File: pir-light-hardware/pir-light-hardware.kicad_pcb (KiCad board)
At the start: 2 copper layers, 29.1 x 32.2 mm, 28 parts, among them J1 ZH1.5-3, J2 ZH1.5-3, Q1 AON7240, U1 M74VHC1GT08DFT2G, U2 LMV331IDCKR

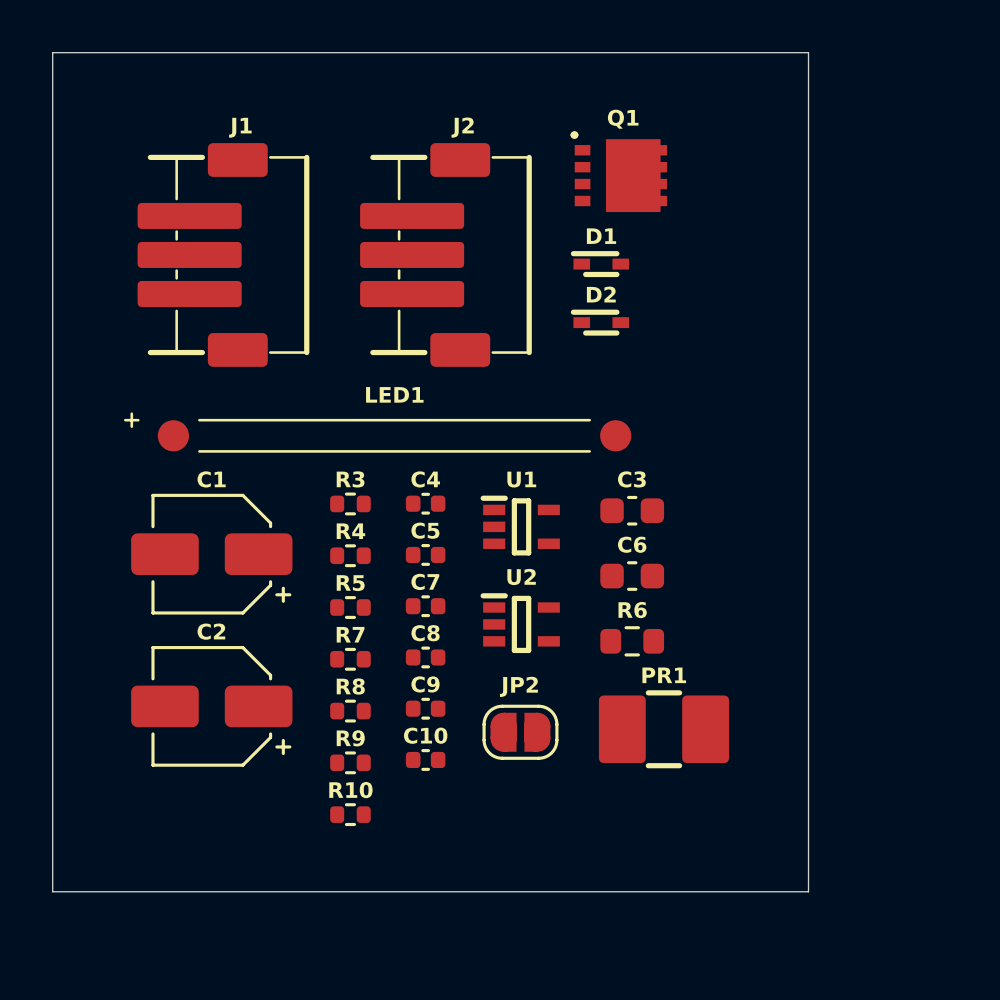
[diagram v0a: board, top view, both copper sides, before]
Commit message: chore: rework sustain feature, add actual components to schematic
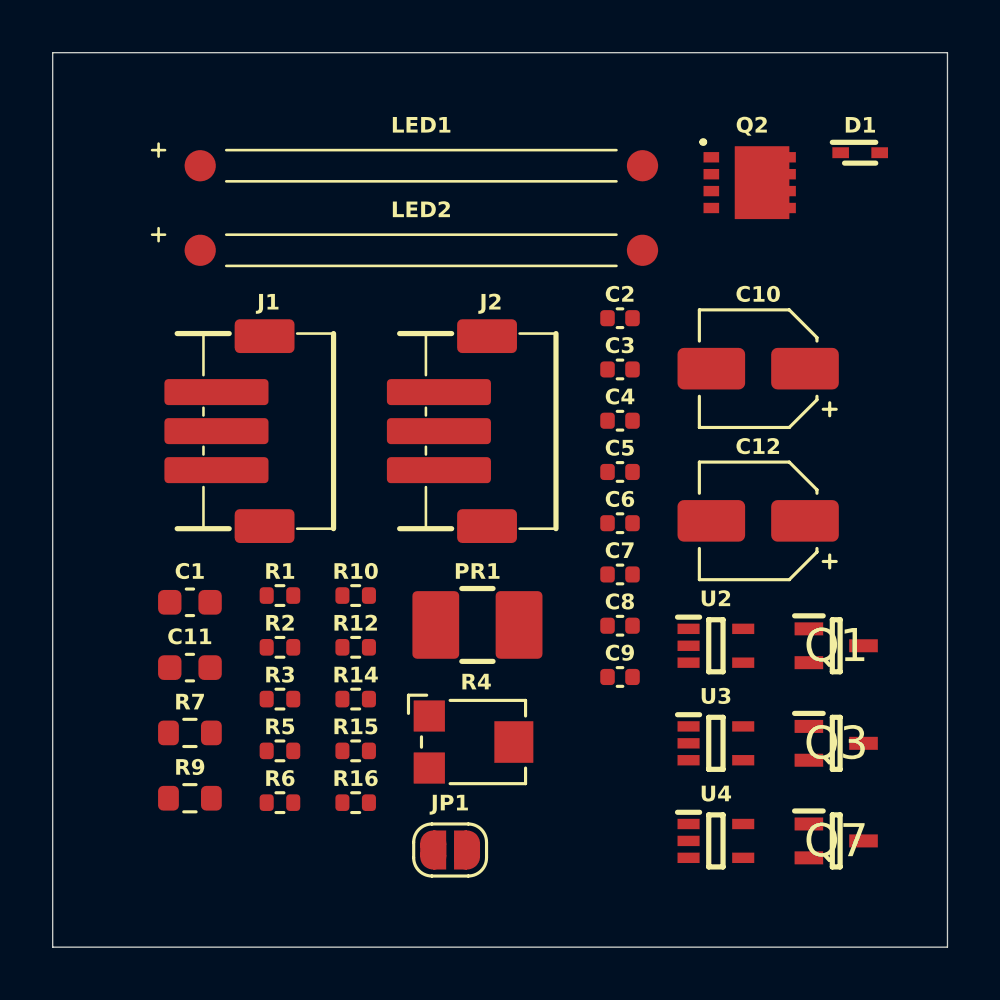
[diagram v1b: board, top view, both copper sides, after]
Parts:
- removed D2: 1N5819HWQ-7-F, 1N5819HWQ-7-F:1N5819HWQ-7-F
- removed JP2: Jumper_Open, REST:SolderJumper-2_P1.3mm_Open_RoundedPad1.0x1.5mm
- removed R8: 10kR, REST:R_0402_1005Metric
- removed U1: M74VHC1GT08DFT2G, M74VHC1GT08D:SOT65P210X110-5N
- added C11: 10uF, REST:C_0603_1608Metric, F.Cu at (181.7, 100.9)
- added C12: 47uF, REST:CP_Elec_4x5.4, F.Cu at (203.6, 95.2)
- added JP1: Jumper_Open, REST:SolderJumper-2_P1.3mm_Open_RoundedPad1.0x1.5mm, F.Cu at (191.7, 107.9)
- added LED2: ~, LED-ROD:LED-ROD, F.Cu at (190.6, 84.8)
- added Q2: AON7240, AON7240:AON7240, F.Cu at (203.3, 82.2)
- added Q3: DTA114EUAHE3-TP, DTA114EUAHE3-TP:SOT65P228X120-3N, F.Cu at (206.6, 103.8)
- added Q7: DTA114EUAHE3-TP, DTA114EUAHE3-TP:SOT65P228X120-3N, F.Cu at (206.6, 107.5)
- added R1: 100kR, REST:R_0402_1005Metric, F.Cu at (185.2, 98.1)
- added R12: 620kR, REST:R_0402_1005Metric, F.Cu at (188.1, 100.1)
- added R14: 47kR, REST:R_0402_1005Metric, F.Cu at (188.1, 102.1)
- added R15: 1MR, REST:R_0402_1005Metric, F.Cu at (188.1, 104.1)
- added R16: 1MR, REST:R_0402_1005Metric, F.Cu at (188.1, 106.1)
- added R2: 100kR, REST:R_0402_1005Metric, F.Cu at (185.2, 100.1)
- added U3: LMV331IDCKR, M74VHC1GT08D:SOT65P210X110-5N, F.Cu at (201.9, 103.8)
- added U4: LMV331IDCKR, M74VHC1GT08D:SOT65P210X110-5N, F.Cu at (201.9, 107.5)
- C1: value 33uF -> 10uF; footprint REST:CP_Elec_4x5.4 -> REST:C_0603_1608Metric
- C10: value 100nF -> 33uF; footprint REST:C_0402_1005Metric -> REST:CP_Elec_4x5.4
- C2: value 47uF -> 100nF; footprint REST:CP_Elec_4x5.4 -> REST:C_0402_1005Metric
- C3: value 10uF -> 10nF; footprint REST:C_0603_1608Metric -> REST:C_0402_1005Metric
- C4: value 10nF -> 100nF
- C6: value 10uF -> 100nF; footprint REST:C_0603_1608Metric -> REST:C_0402_1005Metric
- Q1: value AON7240 -> DTC114EUA-TP; footprint AON7240:AON7240 -> DTC114EUA-TP:SOT65P228X120-3N
- R10: value R -> 10kR
- R4: value 620kR -> 200kR; footprint REST:R_0402_1005Metric -> REST:Potentiometer_Bourns_TC33X_Vertical
- R5: value 1MR -> 10kR
- R6: value 0R -> R; footprint REST:R_0603_1608Metric -> REST:R_0402_1005Metric
- R7: value 100kR -> 0R; footprint REST:R_0402_1005Metric -> REST:R_0603_1608Metric
- R9: value R -> 0R; footprint REST:R_0402_1005Metric -> REST:R_0603_1608Metric
- U2: value LMV331IDCKR -> M74VHC1GT08DFT2G
- moved C2 21.7 mm to (198.2, 87.4)
- moved Q1 19.8 mm to (206.6, 100.0)
- moved C10 19.7 mm to (203.6, 89.4)
- moved R6 14.9 mm to (185.2, 106.1)
- moved D1 10.8 mm to (207.5, 81.1)
- moved LED1 10.4 mm to (190.6, 81.6)
- moved R4 8.64 mm to (192.7, 103.7)
- moved R10 8.42 mm to (188.1, 98.1)
- moved PR1 8.22 mm to (192.8, 99.2)
- moved C4 8.12 mm to (198.2, 91.4)
- moved C5 8.12 mm to (198.2, 93.3)
- moved R3 7.97 mm to (185.2, 102.1)
- moved C7 7.57 mm to (198.2, 97.3)
- moved C8 7.57 mm to (198.2, 99.3)
- moved C9 7.57 mm to (198.2, 101.2)
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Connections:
- C1 pad 1: Net-(D1-K) -> 3V3
- C10 pad 1: 3V3 -> Net-(Q3-OUT)
- C3 pad 1: Net-(JP2-A) -> /PIR
- C4 pad 1: /PIR -> 3V3
- C5 pad 1: 3V3 -> /ALT
- C6 pad 1: 3V3 -> /ALV
- C7 pad 1: /REF -> /FBT
- C8 pad 1: /LLS -> 3V3
- D1 pad 1: Net-(D1-K) -> /STL
- J1 pad 1: /TIN -> GND
- J1 pad 2: 3V3 -> VIN
- J1 pad 3: GND -> /STL
- J2 pad 1: GND -> /STL
- J2 pad 2: 3V3 -> VIN
- J2 pad 3: /TOUT -> GND
- LED1 pad 2: Net-(Q1-D) -> Net-(Q2-D)
- PR1 pad 1: /LLS -> /ALV
- Q1 pad 1: GND -> /STL
- Q1 pad 2: Net-(JP2-A) -> GND
- Q1 pad 3: Net-(Q1-D) -> Net-(Q1-OUT)
- R10 pad 1: /REF -> 3V3
- R10 pad 2: GND -> Net-(Q7-GND)
- R3 pad 1: Net-(D1-K) -> 3V3
- R3 pad 2: GND -> /FBT
- R4 pad 1: Net-(D1-K) -> GND
- R4 pad 2: Net-(JP2-A) -> /ALT
- R5 pad 1: Net-(JP2-A) -> /FBT
- R6 pad 1: 3V3 -> /ALT
- R6 pad 2: Net-(LED1-Pad1) -> GND
- R7 pad 2: /LLS -> Net-(LED1-Pad1)
- R9 pad 2: /REF -> Net-(LED2-Pad1)
- U2 pad 1: /LLS -> Net-(Q7-GND)
- U2 pad 2: (no net) -> /PIR
- U2 pad 3: /REF -> GND
- U2 pad 4: GND -> Net-(D1-A)
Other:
- board size 29.1 x 32.2 mm -> 34.4 x 34.4 mm
